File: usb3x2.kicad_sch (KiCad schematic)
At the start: 80 parts

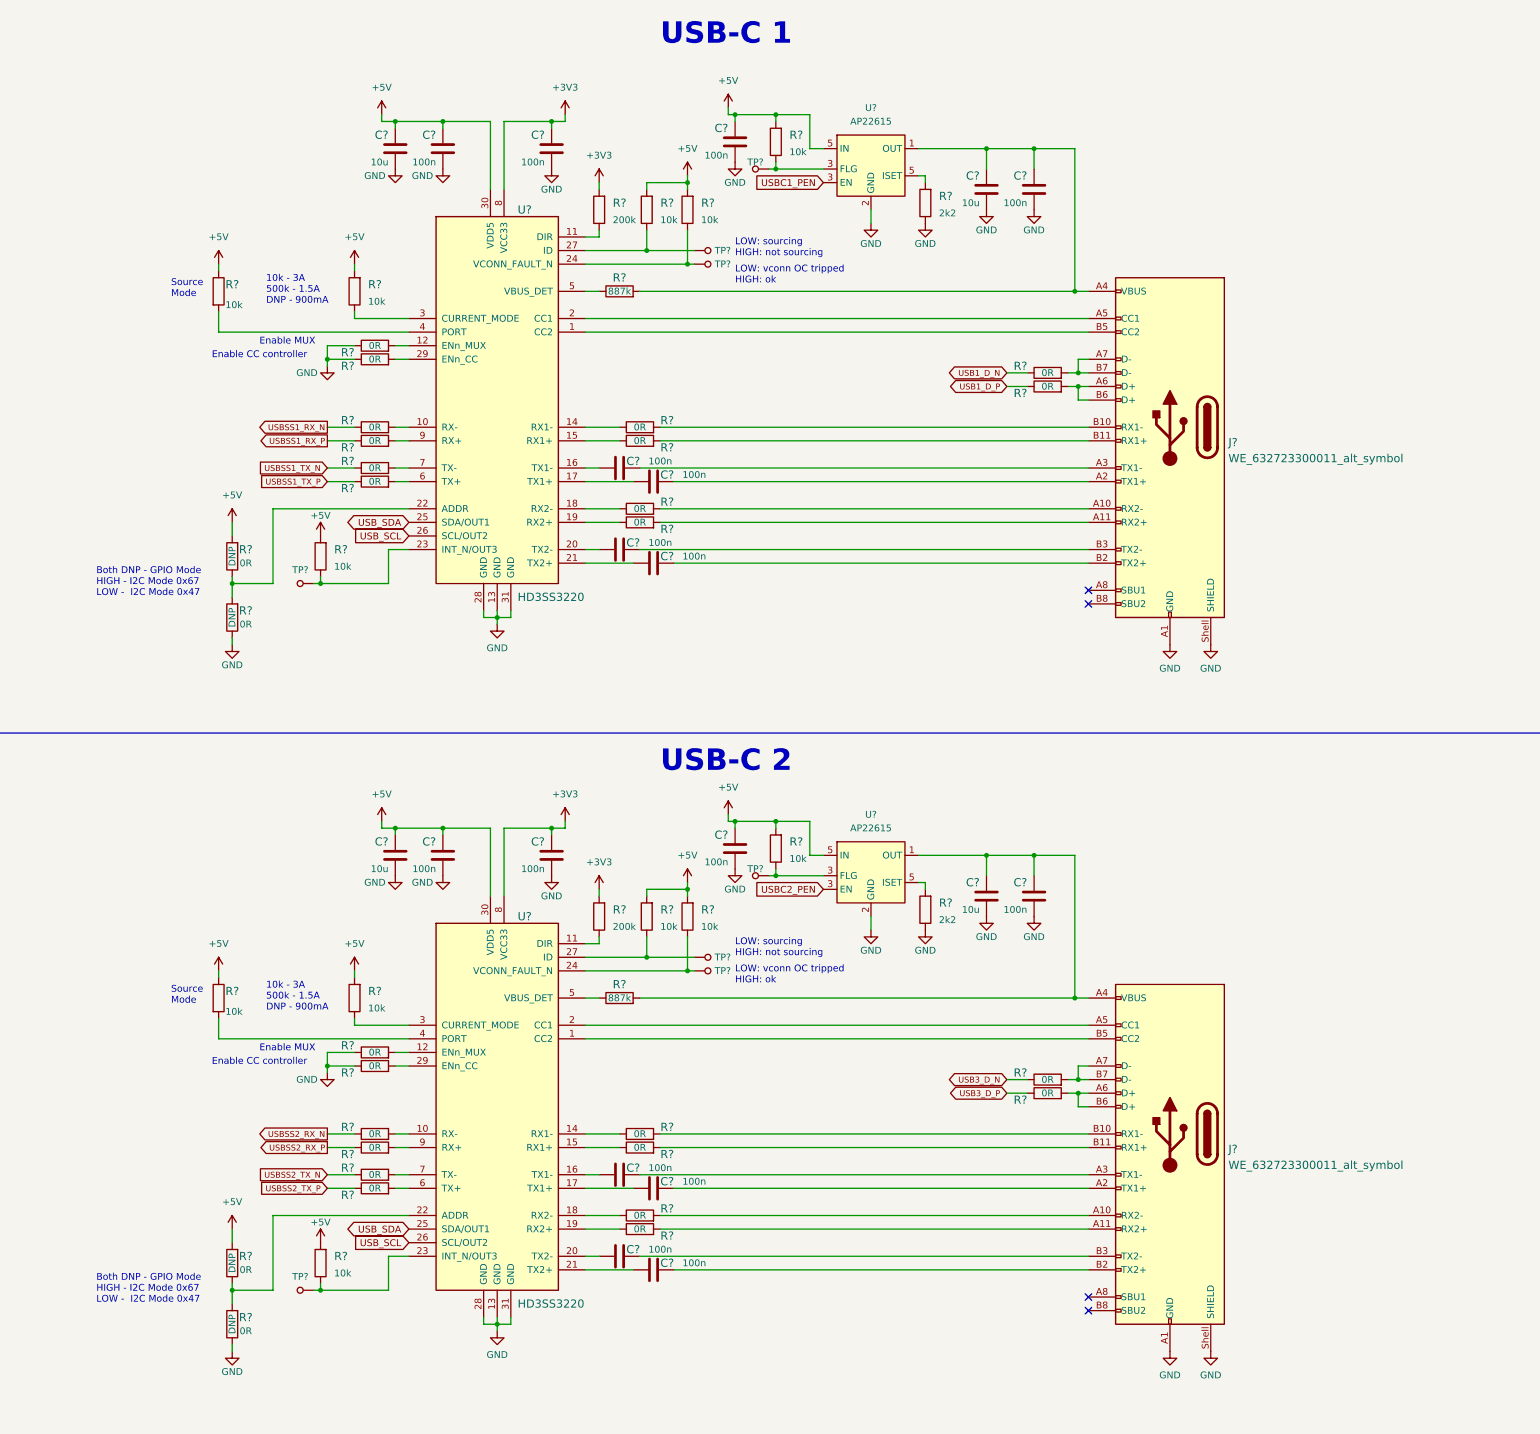
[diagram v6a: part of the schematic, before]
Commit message: Modified USB-C power switch circuitry, added VBUS LED indicator
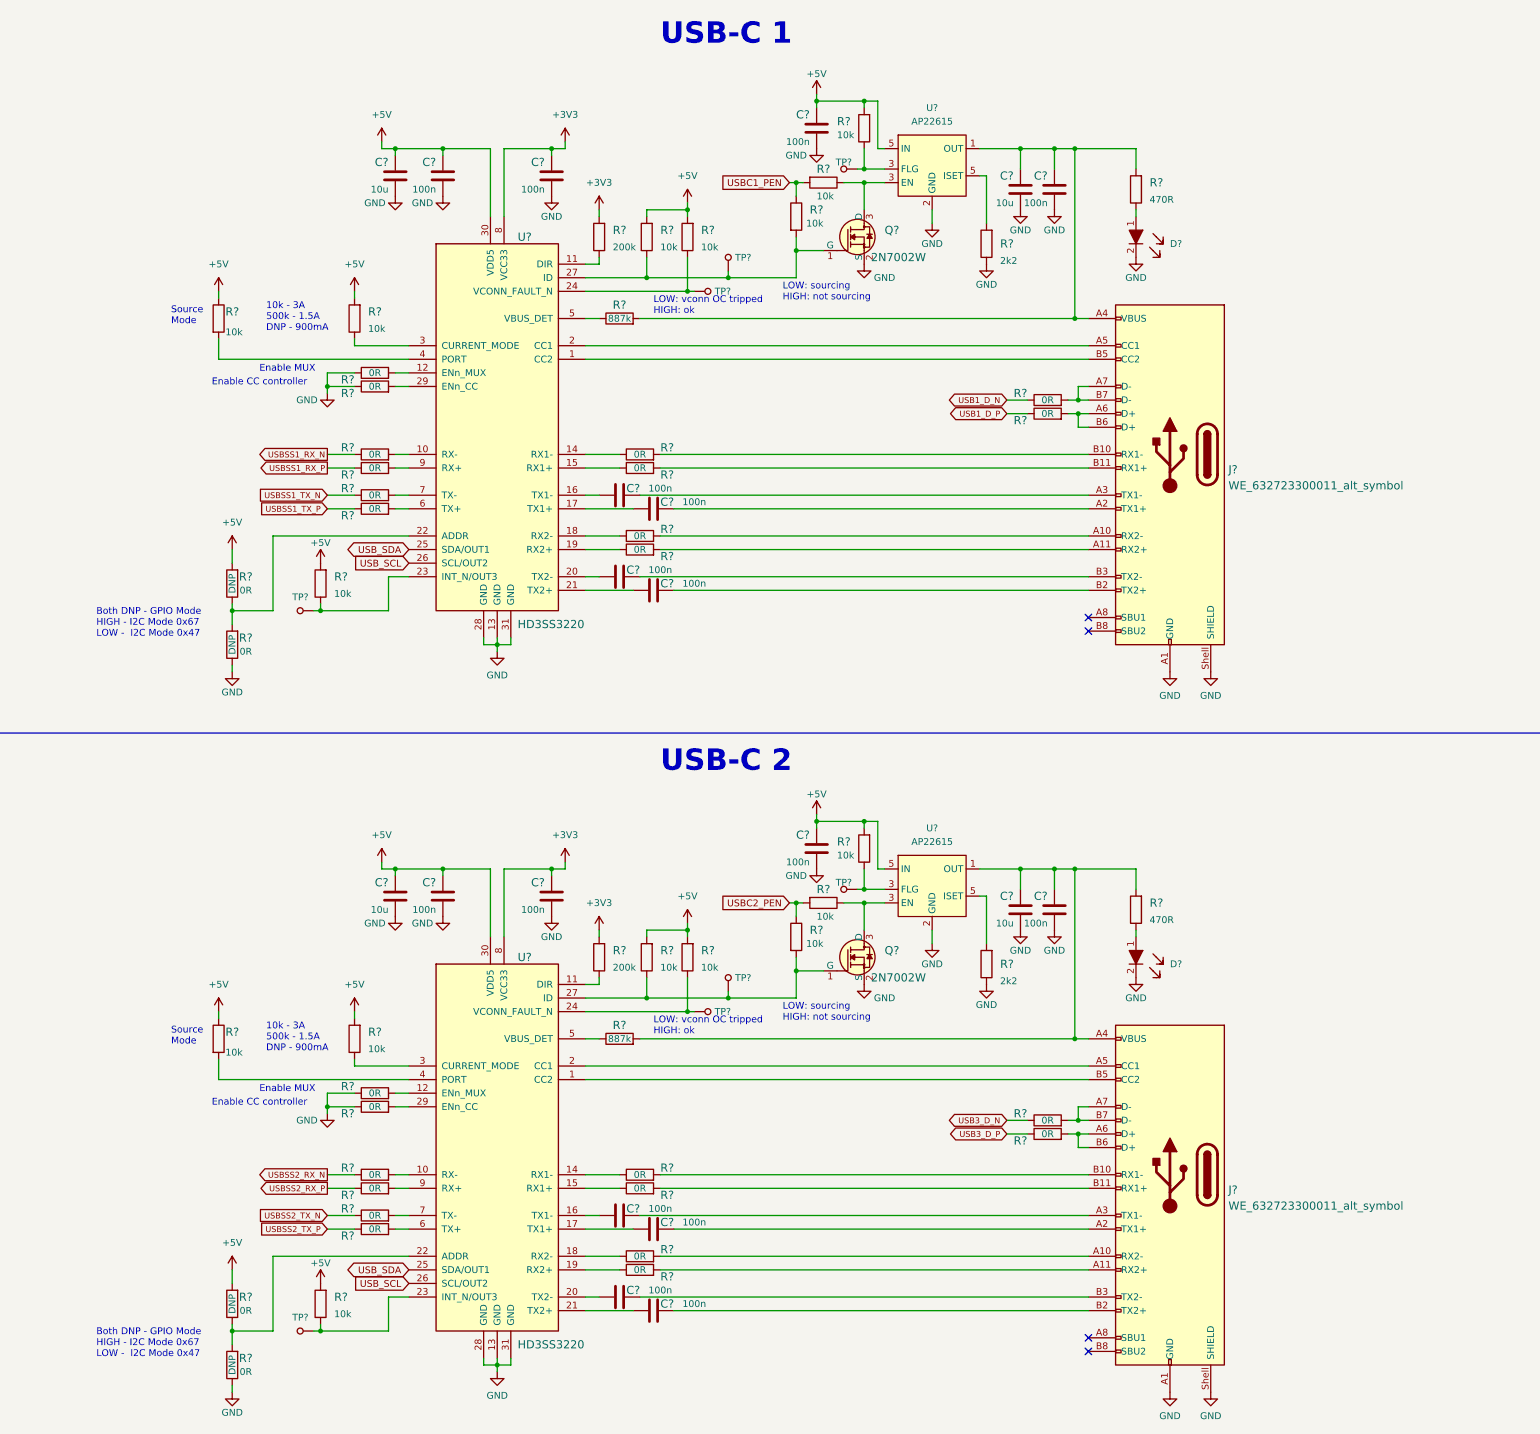
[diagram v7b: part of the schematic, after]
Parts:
- removed C? (x2): C_100n_0402, antmicro-footprints:0402-cap, symbol antmicroCapacitors0402:C_100n_0402
- removed C?: C_10u_0603, antmicro-footprints:0603-cap, symbol antmicroCapacitors0603:C_10u_0603
- removed R?: R_887k_0402, antmicro-footprints:0402-res, symbol antmicroResistors0402:R_887k_0402
- removed R?: R_2k2_0402, antmicro-footprints:0402-res, symbol antmicroResistors0402:R_2k2_0402
- removed R? (x3): R_10k_0402, antmicro-footprints:0402-res, symbol antmicroResistors0402:R_10k_0402
- removed R?: R_200k_0402, antmicro-footprints:0402-res, symbol antmicroResistors0402:R_200k_0402
- removed TP? (x3): TP_SMD_0_75MM, antmicro-footprints:Testpoint_smd_0_75mm, symbol antmicroTestPoints:TP_SMD_0_75MM
- removed U?: AP22615, antmicro-footprints:TSOT23-6, symbol antmicroPMICPowerDistributionSwitchesLoadDrivers:AP22615
- added C? (x2): C_100n_0402, antmicro-footprints:0402-cap, symbol antmicroCapacitors0402:C_100n_0402
- added C?: C_10u_0603, antmicro-footprints:0603-cap, symbol antmicroCapacitors0603:C_10u_0603
- added D? (x2): LTST-C190GKT, crosslink-nx-video-converter-footprints:LED_0603, symbol crosslink-nx-video-converter:LTST-C190GKT
- added Q? (x2): 2N7002W, antmicro-footprints:SOT-323, symbol antmicroTransistorsFETsMOSFETsSingle: 2N7002W
- added R? (x7): R_10k_0402, antmicro-footprints:0402-res, symbol antmicroResistors0402:R_10k_0402
- added R?: R_887k_0402, antmicro-footprints:0402-res, symbol antmicroResistors0402:R_887k_0402
- added R? (x2): R_470R_0603, antmicro-footprints:0603-res, symbol antmicroResistors0603:R_470R_0603
- added R?: R_200k_0402, antmicro-footprints:0402-res, symbol antmicroResistors0402:R_200k_0402
- added R?: R_2k2_0402, antmicro-footprints:0402-res, symbol antmicroResistors0402:R_2k2_0402
- added TP? (x3): TP_SMD_0_75MM, antmicro-footprints:Testpoint_smd_0_75mm, symbol antmicroTestPoints:TP_SMD_0_75MM
- added U?: AP22615, antmicro-footprints:TSOT23-6, symbol antmicroPMICPowerDistributionSwitchesLoadDrivers:AP22615
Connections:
- net +3V3: now also R?.2
- net +5V: now also C?.1, R?.2, R?.2, R?.2, U?.5 (ISET)
- net GND: now also C?.2, C?.2, C?.2, D?.2, D?.2, Q?.2 (S), Q?.2 (S), R?.1, U?.2 (GND)
- net USBC1_PEN: now also R?.1, R?.2; no longer U?.3 (FLG)
- net USBC2_PEN: now also R?.1, R?.2
- net at U?.24 (VCONN_FAULT_N): now also R?.1, TP?.1
- net at U?.5 (VBUS_DET): now also R?.1
- net at J?.A4 (VBUS), J?.A9 (VBUS), J?.B4 (VBUS)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: now also C?.1, C?.1, R?.2, R?.2, U?.1 (OUT)
- net at R?.1, TP?.1, U?.27 (ID): now also Q?.1 (G), R?.2
- net at C?.1, C?.1, J?.A4 (VBUS)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: now also R?.2
- net at U?.11 (DIR): now also R?.1
- net at U?.27 (ID): now also Q?.1 (G), R?.1, R?.2, TP?.1
- new net: Q?.3 (D), R?.1, U?.3 (FLG) (x2)
- new net: R?.1, TP?.1, U?.3 (FLG)
- new net: R?.2, U?.5 (ISET)
- new net: D?.1, R?.1 (x2)
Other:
- moved on the sheet: C?, J?, R?, TP?, U?
